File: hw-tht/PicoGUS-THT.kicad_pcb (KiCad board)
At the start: 2 copper layers, 103.7 x 99.8 mm, 78 parts, among them J1 IRQDMA_JP, J2 ISA debug (DNP), J3 Bus_ISA_8bit, J5 SJ1-3535NG, J6 UART_TX, J7 USB power jumper, J8 SJ1-3535NG-GR, J9 Waveblaster, U1 Pico, U10 74AHCT126, U11 NE5532, U2 74AHC244, U3 SN74CB3T3257, U4 SN74CB3T3257, U5 74AHC14, U6 74AHC00, U7 74AHC00, U8 APS6404L-3SQR-SN, U9 PCM5100A

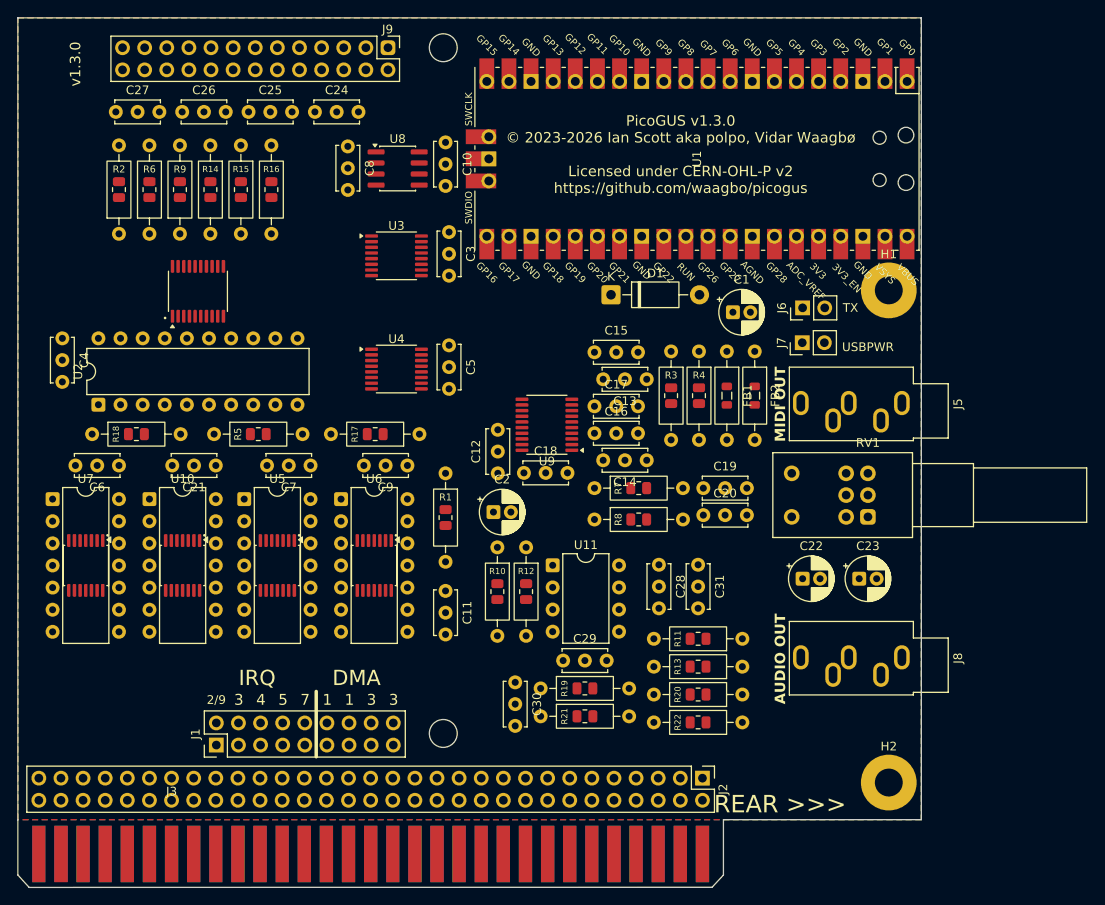
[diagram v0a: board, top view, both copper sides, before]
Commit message: hw-tht: 5 mm disc/0805 hybrid capacitors, labels inside or beside bodies
- New C_Disc_D5.0mm_W2.5mm_P5.00mm_0805_Hybrid footprint for all ceramic
  caps: 5.0/5.08 mm radial part OR an 0805 between the holes. Replaces
  the 2.5/5.0 mm dual-pitch footprint.
- BOM: every ceramic cap line is now 5 mm pitch at both distributors
  (2.2 nF LCSC Dersonic C22391154, 100 pF DigiKey Vishay
  K101J15C0GF5TH5) and lists an in-stock 0805 alternative.
- Silkscreen labels: FB1/FB2 inside the body like the resistors;
  capacitor labels just outside the body, above/left, else at a free end.

Co-Authored-By: Claude Opus 5.5 <noreply@anthropic.com>
Claude-Session: https://claude.ai/code/session_011utN3x8yYUNDvkpGCEq5yD
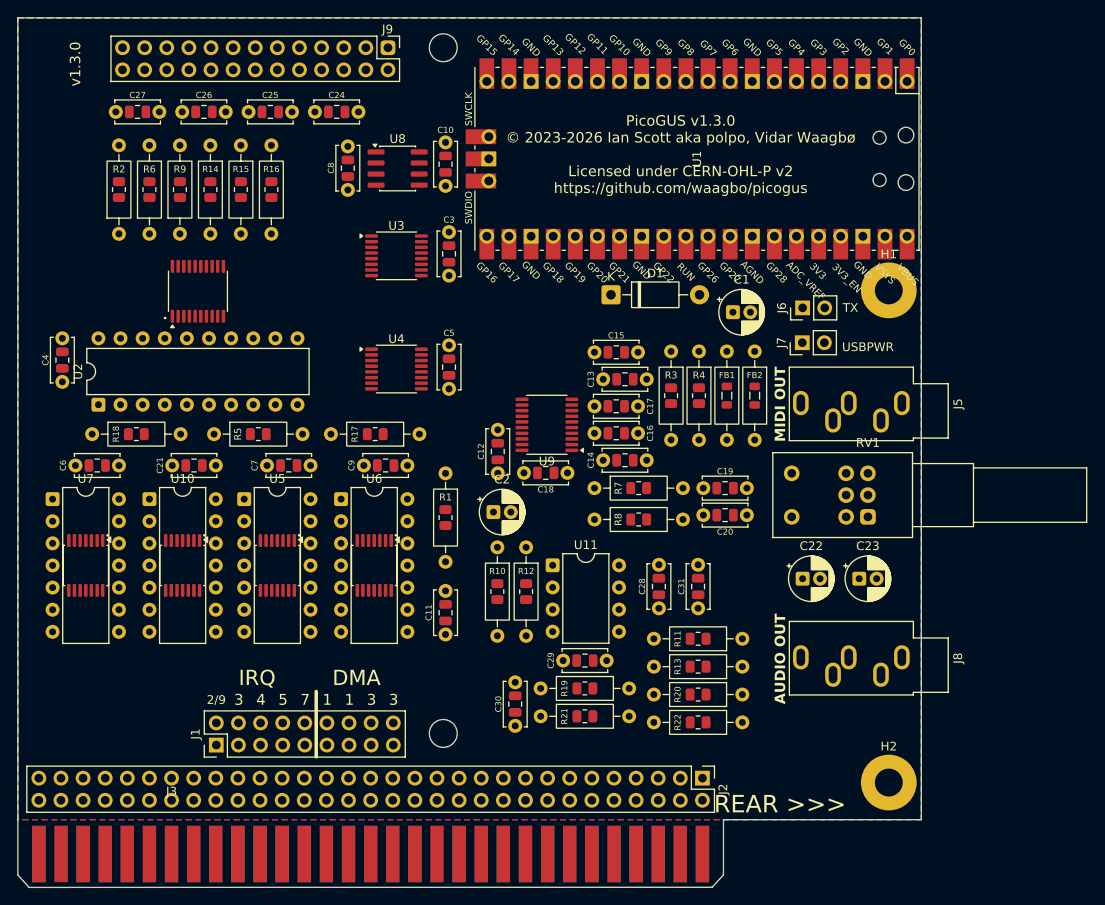
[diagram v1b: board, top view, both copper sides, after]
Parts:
- C10, C11, C12, C13, C14, C15, C16, C17, C18, C19, C20, C21, C24, C25, C26, C27, C28, C29, C3, C30, C31, C4, C5, C6, C7, C8, C9: footprint PicoGUS-THT:C_Disc_D5.0mm_W2.5mm_P2.50mm_P5.00mm -> PicoGUS-THT:C_Disc_D5.0mm_W2.5mm_P5.00mm_0805_Hybrid

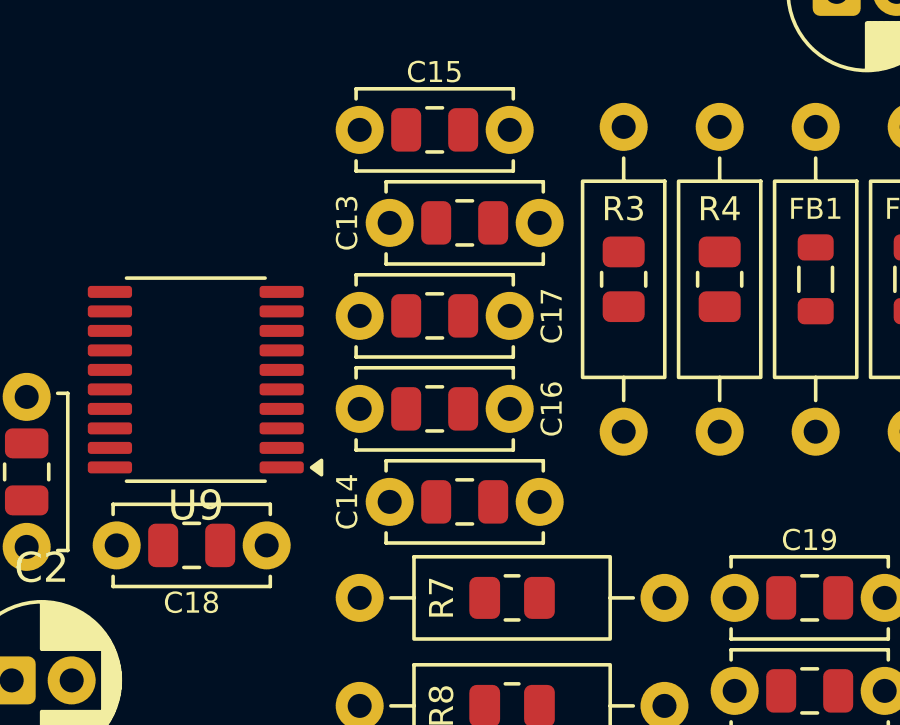
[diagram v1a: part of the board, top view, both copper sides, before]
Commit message: hw-tht: align the DAC capacitor stack
C13 and C14 now use the same hole positions as C15, C16 and C17
(x 182.6 / 187.6), with their 3.3 V pad still facing U9; the stack's
labels all sit at the right-hand end.

Co-Authored-By: Claude Opus 5.5 <noreply@anthropic.com>
Claude-Session: https://claude.ai/code/session_011utN3x8yYUNDvkpGCEq5yD
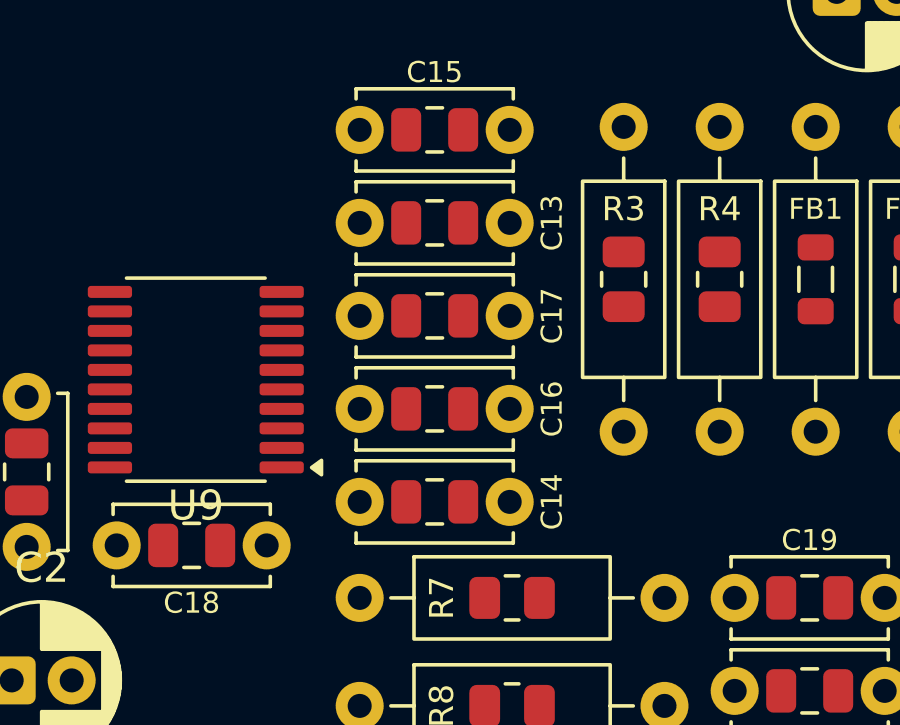
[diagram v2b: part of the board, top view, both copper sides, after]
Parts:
- moved C13 1.00 mm to (187.6, 77.7)
- moved C14 1.00 mm to (187.6, 87.0)

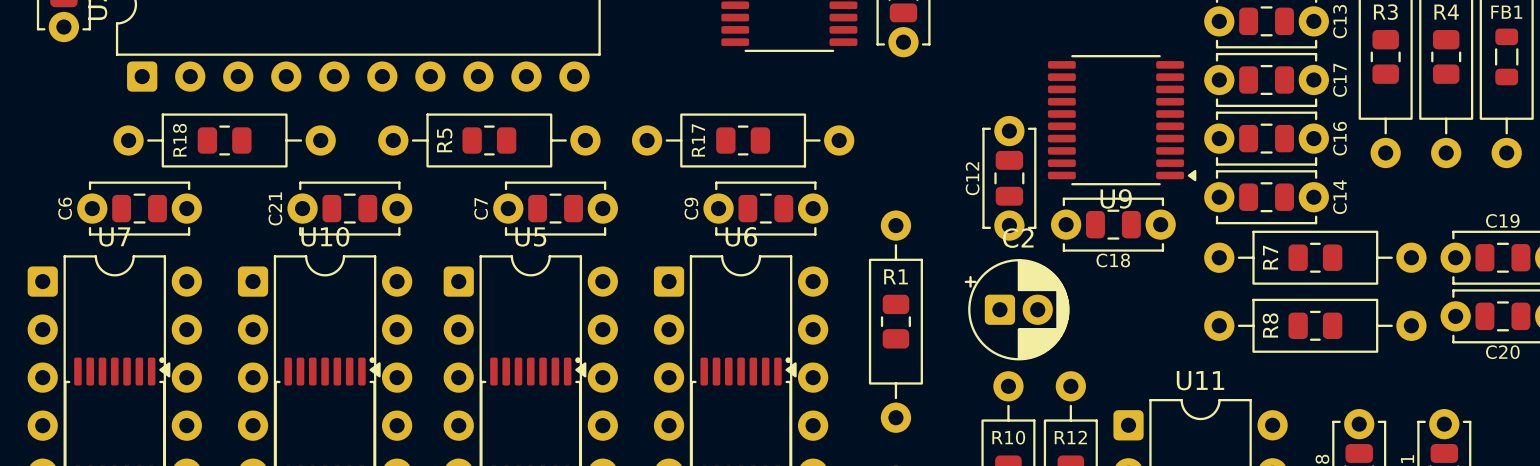
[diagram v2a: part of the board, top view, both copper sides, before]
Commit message: hw-tht: R7/R8 side by side like C19/C20
The axial/0805 resistor hybrid keeps the standard axial courtyard
(which already covers the 0805 pads) instead of a larger bounding box,
so resistors pack at the same 3.1 mm row pitch as the capacitors.
R8 now sits on C20's row, directly under R7.

Co-Authored-By: Claude Opus 5.5 <noreply@anthropic.com>
Claude-Session: https://claude.ai/code/session_011utN3x8yYUNDvkpGCEq5yD
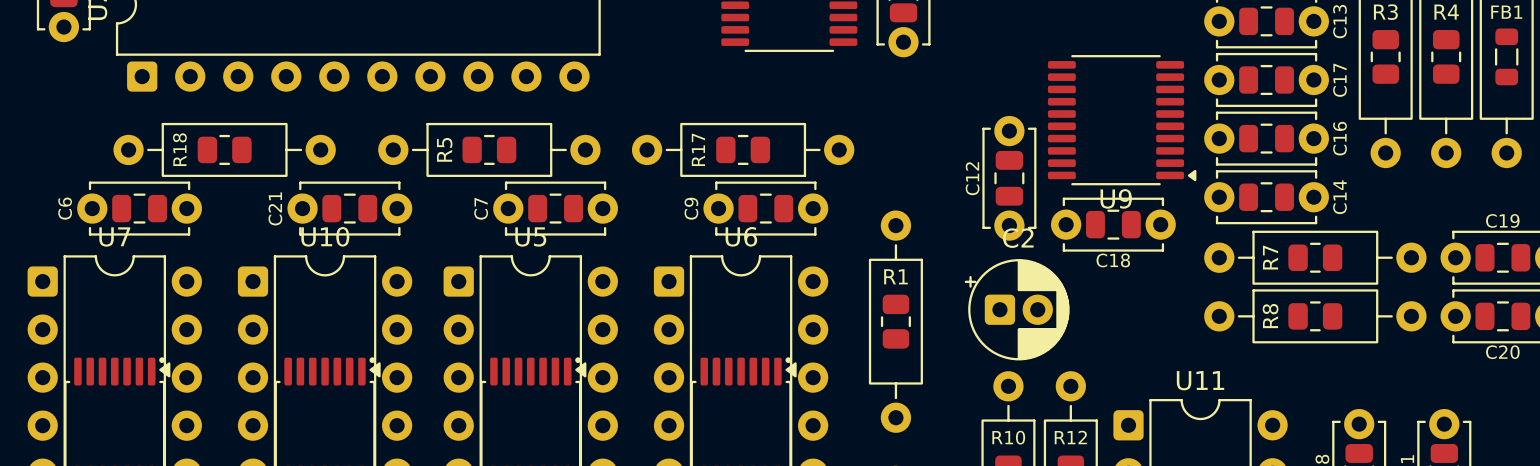
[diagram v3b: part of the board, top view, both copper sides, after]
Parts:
- moved R17 0.50 mm to (162.5, 84.5)
- moved R18 0.50 mm to (124.9, 84.5)
- moved R5 0.50 mm to (138.9, 84.5)
- moved R8 0.50 mm to (182.6, 93.3)

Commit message: hw-tht: remove the J2 ISA debug header, move U3/U4 to the gold fingers
- J2 (2x31 ISA probe header, never fitted, carried over from v1.2) is
  removed from schematic, board and BOM. Its 62 pads formed a wall just
  above the fingers that every ISA signal had to cross, which kept the
  autorouter stuck. ISA pins that only went to J2 get no-connect flags.
- U3/U4 (CB3T3257 bus switches) sit in the freed strip right above the
  data-line fingers, with C3/C5 2.5 mm from their supply pins; their 16
  ISA-side lines are now short, only the 8 AD lines run to the Pico.
- Power tracks: +5V/+3V3/VSYS 0.4 mm (was 0.5 mm, barely fit between
  DIP pins); +/-12V use normal 0.25 mm tracks (a few mA).

Co-Authored-By: Claude Opus 5.5 <noreply@anthropic.com>
Claude-Session: https://claude.ai/code/session_011utN3x8yYUNDvkpGCEq5yD
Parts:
- removed J2: ISA debug (DNP), Connector_PinHeader_2.54mm:PinHeader_2x31_P2.54mm_Vertical
- moved U3 62.6 mm to (172.0, 124.9)
- moved C3 60.2 mm to (175.5, 120.2), turned to 0 degrees
- moved U4 54.3 mm to (184.5, 124.9)
- moved C5 51.4 mm to (188.0, 120.2), turned to 0 degrees
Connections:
- J3 pad 11: Net-(J2-Pin_11) -> (no net)
- J3 pad 12: Net-(J2-Pin_12) -> (no net)
- J3 pad 19: Net-(J2-Pin_19) -> (no net)
- J3 pad 20: Net-(J2-Pin_20) -> (no net)
- J3 pad 22: Net-(J2-Pin_22) -> (no net)
- J3 pad 26: Net-(J2-Pin_26) -> (no net)
- J3 pad 28: Net-(J2-Pin_28) -> (no net)
- J3 pad 30: Net-(J2-Pin_30) -> (no net)
- J3 pad 32: Net-(J2-Pin_32) -> (no net)
- J3 pad 43: Net-(J2-Pin_43) -> (no net)
- J3 pad 44: Net-(J2-Pin_44) -> (no net)
- J3 pad 45: Net-(J2-Pin_45) -> (no net)
- J3 pad 46: Net-(J2-Pin_46) -> (no net)
- J3 pad 47: Net-(J2-Pin_47) -> (no net)
- J3 pad 48: Net-(J2-Pin_48) -> (no net)
- J3 pad 49: Net-(J2-Pin_49) -> (no net)
- J3 pad 5: Net-(J2-Pin_5) -> (no net)
- J3 pad 50: Net-(J2-Pin_50) -> (no net)
- J3 pad 51: Net-(J2-Pin_51) -> (no net)
- J3 pad 52: Net-(J2-Pin_52) -> (no net)
- J3 pad 6: Net-(J2-Pin_6) -> (no net)
- J3 pad 8: Net-(J2-Pin_8) -> (no net)

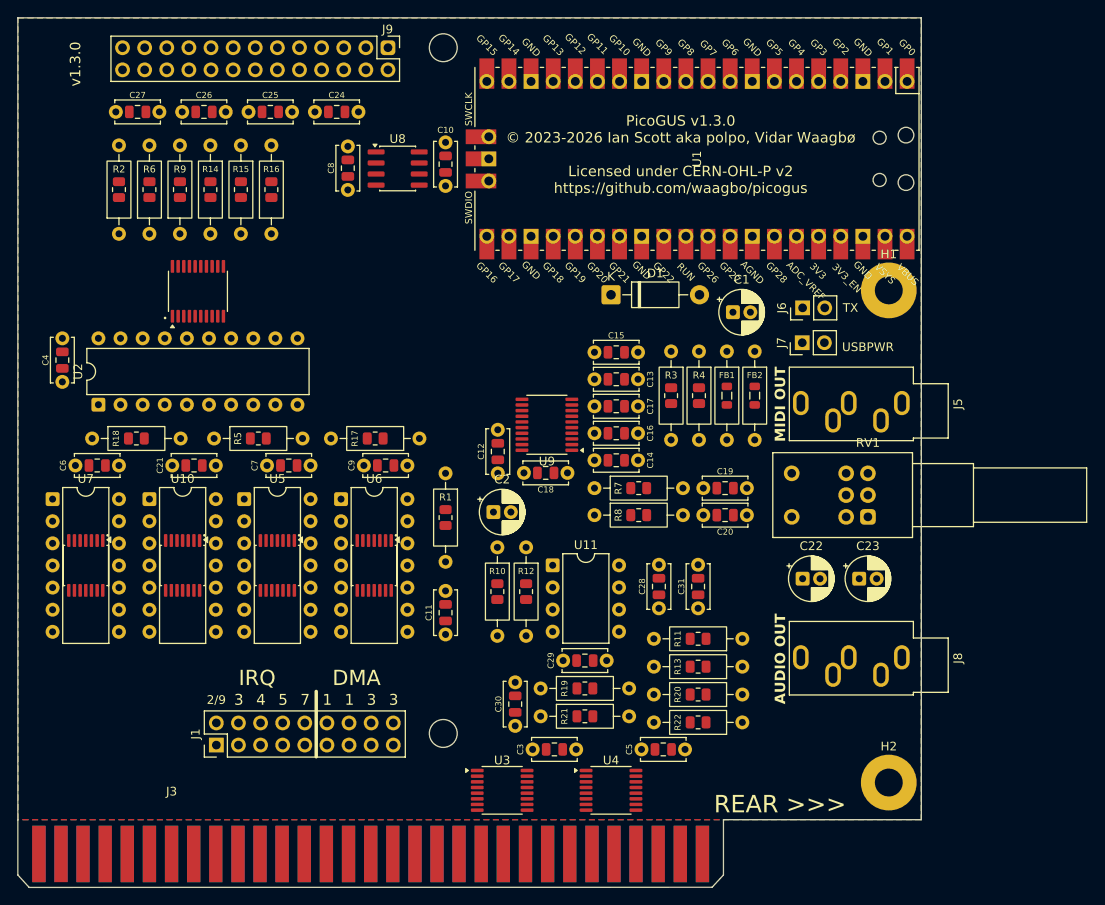
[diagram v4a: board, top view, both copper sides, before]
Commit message: hw-tht: through-hole parts only, drop the hybrid footprints
- Resistors: plain axial DIN0207 (10.16 mm); ceramic caps: plain 5 mm
  disc; FB1/FB2: axial bead on leads (12.7 mm, Fair-Rite 2743002112 /
  LCSC FH RH3.5x0.8x9P52E); logic ICs: plain DIP-14/DIP-20.
- Only the parts that have no THT version stay SMD: U3/U4 (CB3T3257),
  U8 (APS6404L PSRAM), U9 (PCM510x DAC).
- BOM: 0805/TSSOP alternatives removed. The DIP logic ICs are DigiKey
  parts; LCSC has almost none in stock (listed with their real stock).
- Placement from the latest layout review (DIPs in one column, DAC and
  its caps next to the bus switches), FB1/FB2 and C19/C20 shifted to fit
  the longer bead footprint. Passive labels centred inside the bodies.

Co-Authored-By: Claude Opus 5.5 <noreply@anthropic.com>
Claude-Session: https://claude.ai/code/session_011utN3x8yYUNDvkpGCEq5yD
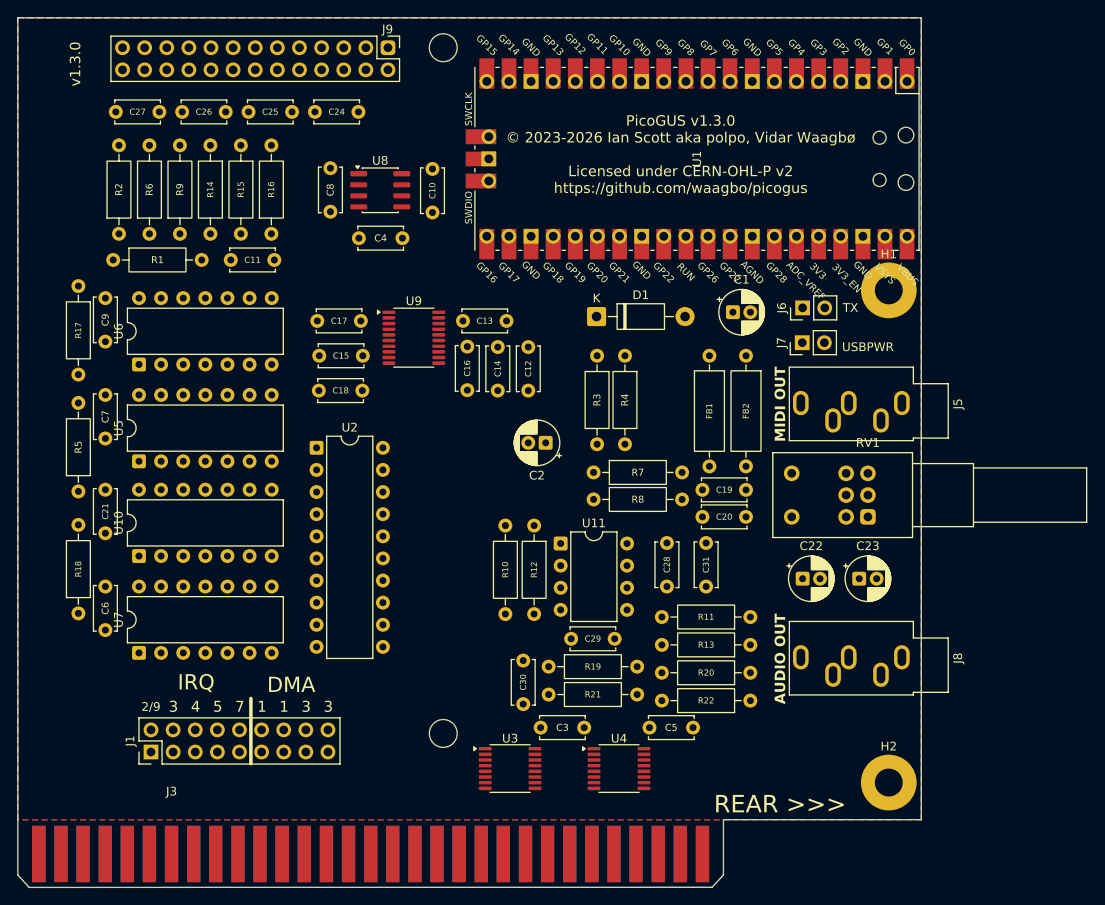
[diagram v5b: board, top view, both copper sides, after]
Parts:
- C10, C11, C12, C13, C14, C15, C16, C17, C18, C19, C20, C21, C24, C25, C26, C27, C28, C29, C3, C30, C31, C4, C5, C6, C7, C8, C9: footprint PicoGUS-THT:C_Disc_D5.0mm_W2.5mm_P5.00mm_0805_Hybrid -> Capacitor_THT:C_Disc_D5.0mm_W2.5mm_P5.00mm
- FB1, FB2: value 1k@100MHz -> Ferrite bead; footprint PicoGUS-THT:FerriteBead_Axial_P10.16mm_0805_Hybrid -> Resistor_THT:R_Axial_DIN0309_L9.0mm_D3.2mm_P12.70mm_Horizontal
- R1, R10, R11, R12, R13, R14, R15, R16, R17, R18, R19, R2, R20, R21, R22, R3, R4, R5, R6, R7, R8, R9: footprint PicoGUS-THT:R_Axial_DIN0207_P10.16mm_0805_Hybrid -> Resistor_THT:R_Axial_DIN0207_L6.3mm_D2.5mm_P10.16mm_Horizontal
- U10, U5, U6, U7: footprint PicoGUS-THT:DIP-14_W7.62mm_TSSOP-14_Hybrid -> Package_DIP:DIP-14_W7.62mm
- U2: footprint PicoGUS-THT:DIP-20_W7.62mm_TSSOP-20_Hybrid -> Package_DIP:DIP-20_W7.62mm
- moved R1 45.3 mm to (127.3, 64.0), turned to 0 degrees
- moved C11 45.3 mm to (140.8, 64.0), turned to 0 degrees
- moved R17 42.9 mm to (123.3, 67.0), turned to -90 degrees
- moved C4 40.7 mm to (160.6, 61.5), turned to 180 degrees
- moved C9 39.6 mm to (126.4, 68.4), turned to -90 degrees
- moved C15 31.6 mm to (151.0, 75.0)
- moved C17 28.6 mm to (155.8, 71.0), turned to 180 degrees
- moved U6 27.9 mm to (130.3, 76.0), turned to 90 degrees
- moved U2 25.5 mm to (150.7, 85.6), turned to 0 degrees
- moved C18 25.4 mm to (150.9, 79.0)
- moved C7 24.9 mm to (126.4, 79.5), turned to -90 degrees
- moved U7 20.3 mm to (130.3, 109.1), turned to 90 degrees
- moved R18 20.1 mm to (123.3, 104.6), turned to 90 degrees
- moved U9 18.3 mm to (161.9, 72.9), turned to 0 degrees
- moved C14 18.0 mm to (171.5, 79.0), turned to 90 degrees
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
